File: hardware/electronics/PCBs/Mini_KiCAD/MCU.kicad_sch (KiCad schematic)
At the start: 21 parts, among them U1 RP2040, U2 W25Q32JVSS

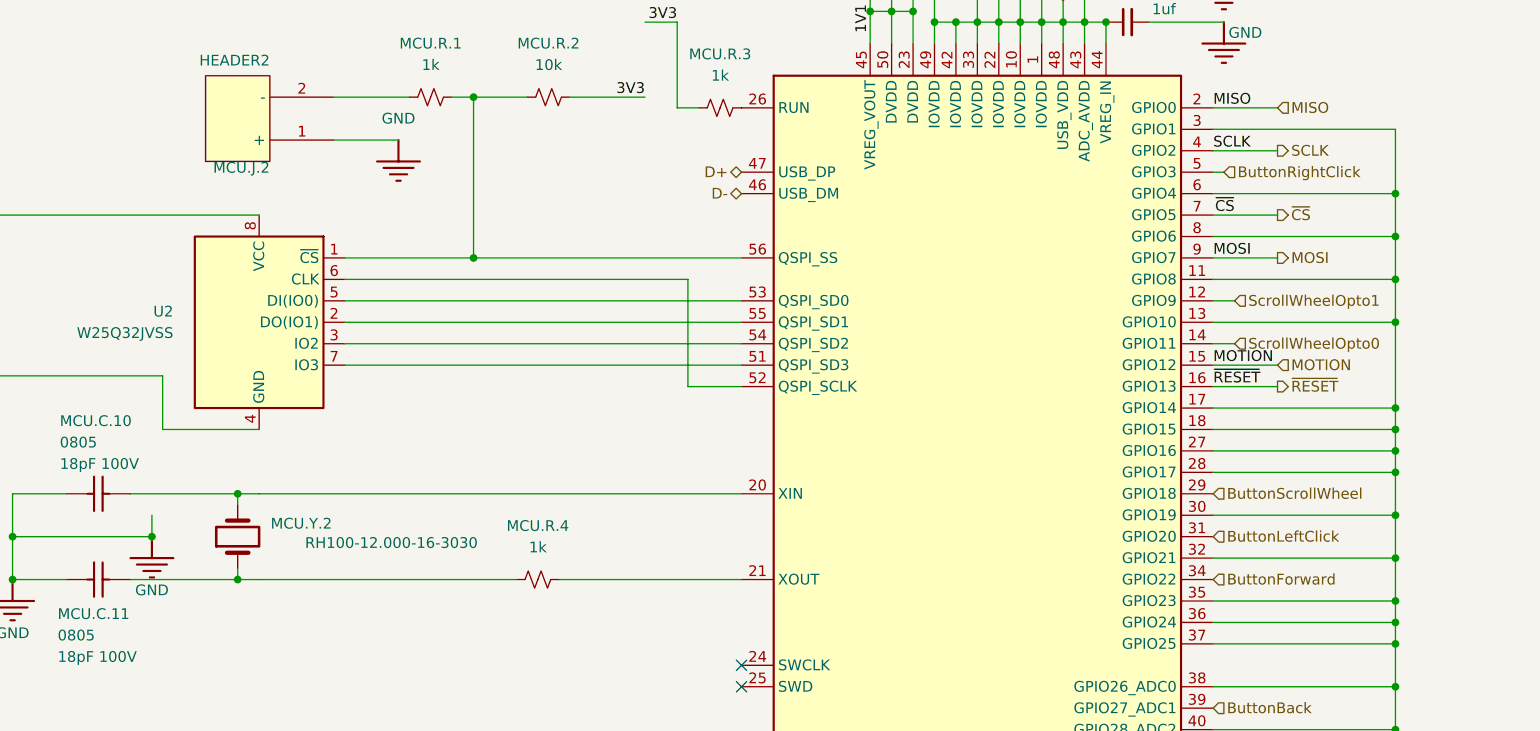
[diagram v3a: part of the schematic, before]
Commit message: Rerouted the SPI devices and general cleanup, relocated all associated footprint library inside the project folder
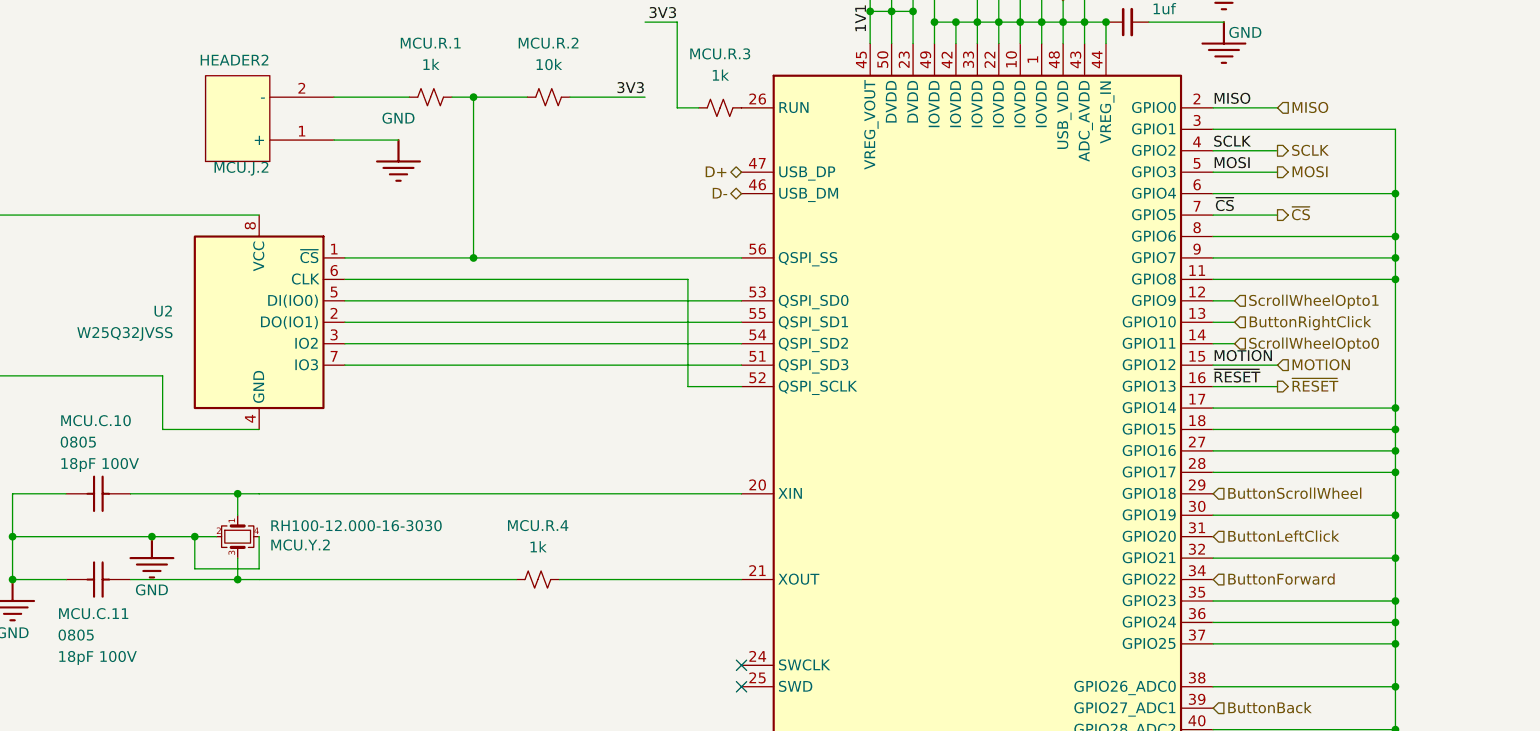
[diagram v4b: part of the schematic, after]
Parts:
- MCU.C.1, MCU.C.13, MCU.C.2, MCU.C.4, MCU.C.5, MCU.C.6, MCU.C.7, MCU.C.8, MCU.C.9: footprint Chip_Passives.PcbLib:0805 -> Chip_Passives.PcbLib:0805 - TALL
- MCU.Y.2: symbol Device:Crystal -> Device:Crystal_GND24_Small
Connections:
- net ButtonRightClick: now also U1.13 (GPIO10); no longer U1.5 (GPIO3)
- net GND: now also MCU.Y.2.2, MCU.Y.2.4, U1.9 (GPIO7); no longer U1.13 (GPIO10)
- net MOSI: now also U1.5 (GPIO3); no longer U1.9 (GPIO7)
- net at MCU.C.10.2, U1.20 (XIN): now also MCU.Y.2.1; no longer MCU.Y.2.2
- net at MCU.C.11.2, MCU.R.4.1: now also MCU.Y.2.3; no longer MCU.Y.2.1

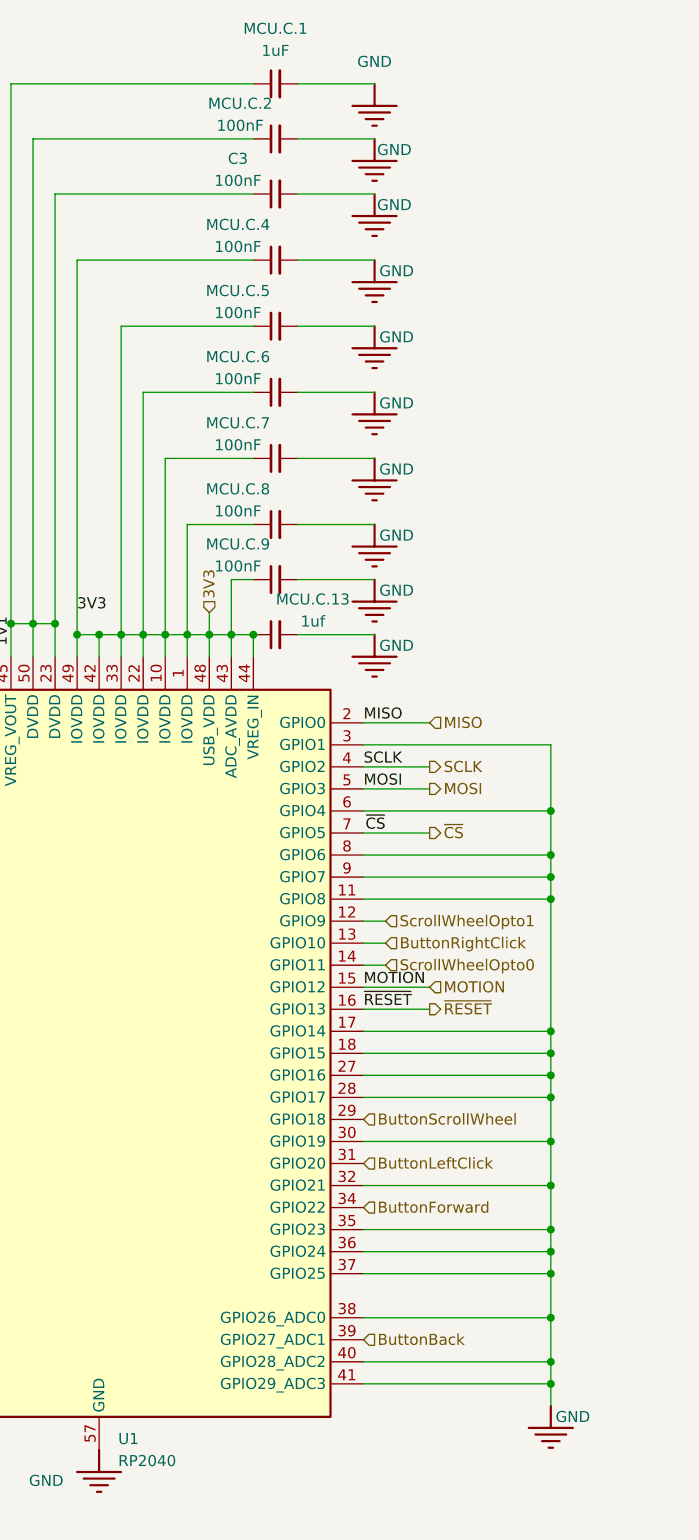
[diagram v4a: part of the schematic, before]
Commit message: Changed button and SPI device pinout to be pin-compatible with the Ploopy Adept.
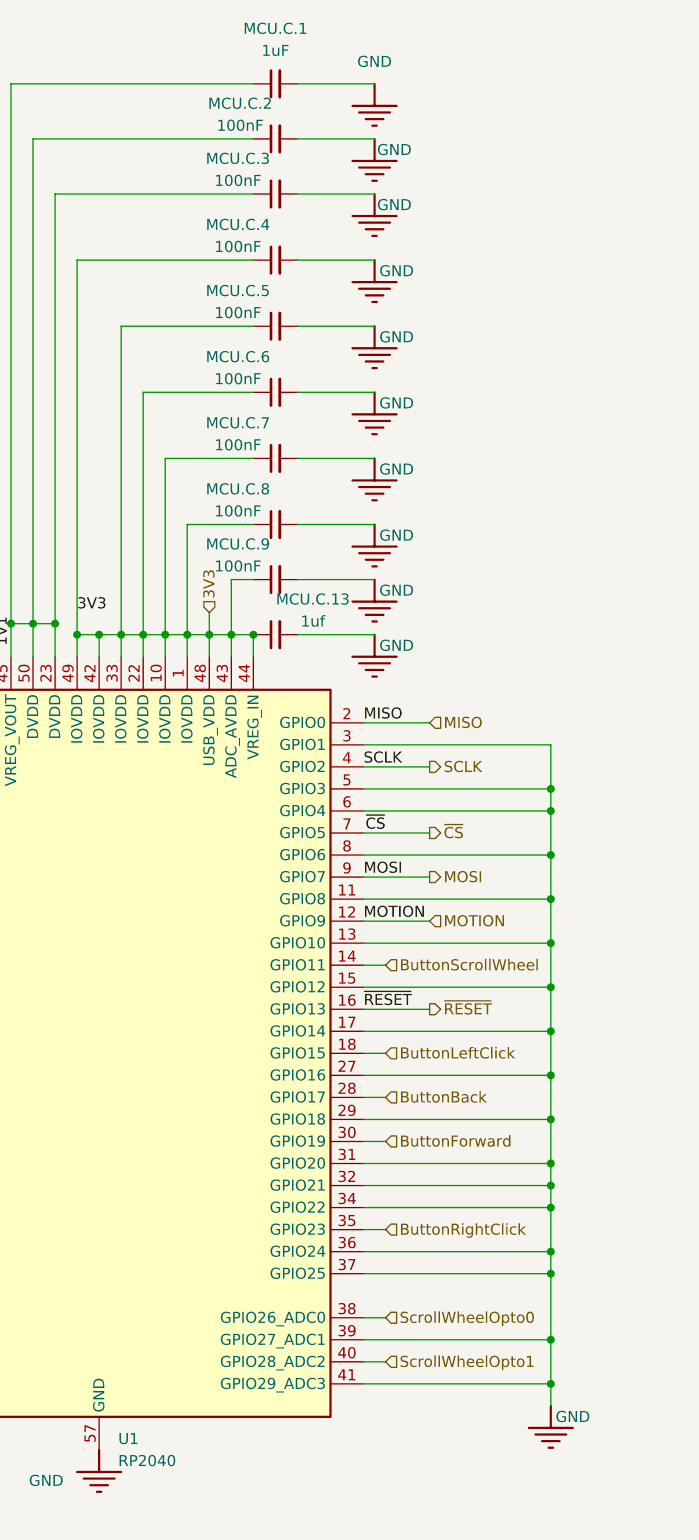
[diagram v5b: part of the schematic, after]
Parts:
- renumbered C3 to MCU.C.3
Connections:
- net ButtonBack: now also U1.28 (GPIO17); no longer U1.39 (GPIO27_ADC1)
- net ButtonForward: now also U1.30 (GPIO19); no longer U1.34 (GPIO22)
- net ButtonLeftClick: now also U1.18 (GPIO15); no longer U1.31 (GPIO20)
- net ButtonRightClick: now also U1.35 (GPIO23); no longer U1.13 (GPIO10)
- net ButtonScrollWheel: now also U1.14 (GPIO11); no longer U1.29 (GPIO18)
- net GND: now also U1.13 (GPIO10), U1.15 (GPIO12), U1.29 (GPIO18), U1.31 (GPIO20), U1.34 (GPIO22), U1.39 (GPIO27_ADC1), U1.5 (GPIO3); no longer U1.18 (GPIO15), U1.28 (GPIO17), U1.30 (GPIO19), U1.35 (GPIO23), U1.38 (GPIO26_ADC0), U1.40 (GPIO28_ADC2), U1.9 (GPIO7)
- net MOSI: now also U1.9 (GPIO7); no longer U1.5 (GPIO3)
- net MOTION: now also U1.12 (GPIO9); no longer U1.15 (GPIO12)
- net ScrollWheelOpto0: now also U1.38 (GPIO26_ADC0); no longer U1.14 (GPIO11)
- net ScrollWheelOpto1: now also U1.40 (GPIO28_ADC2); no longer U1.12 (GPIO9)

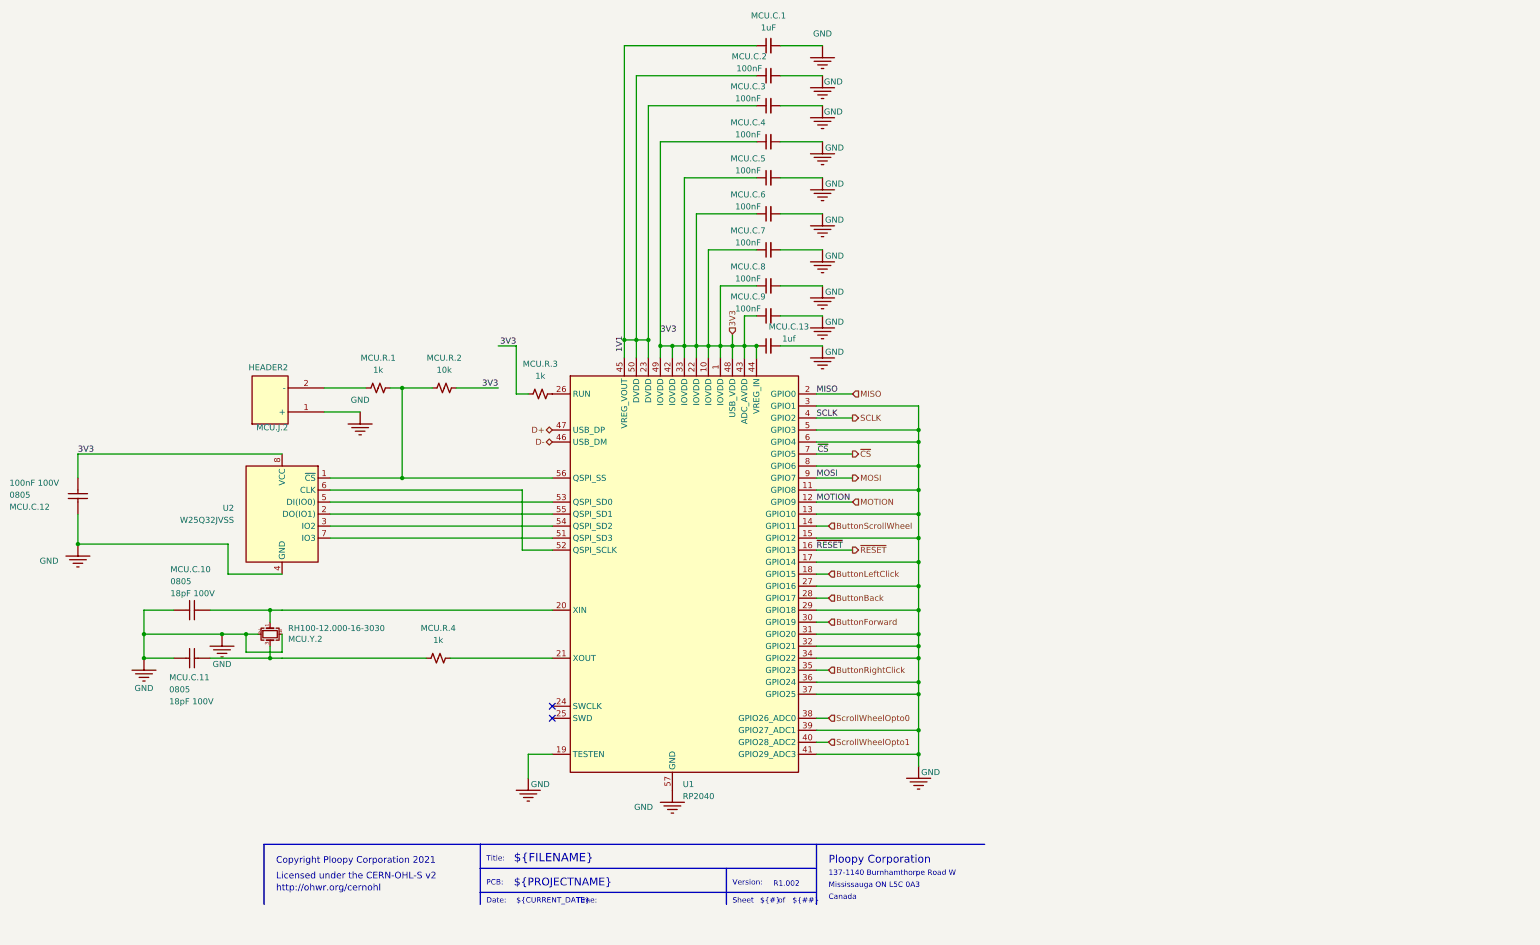
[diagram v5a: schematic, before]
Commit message: Resolved most DRC errors and re-annotated the schematic to be friendly to BOM generation.
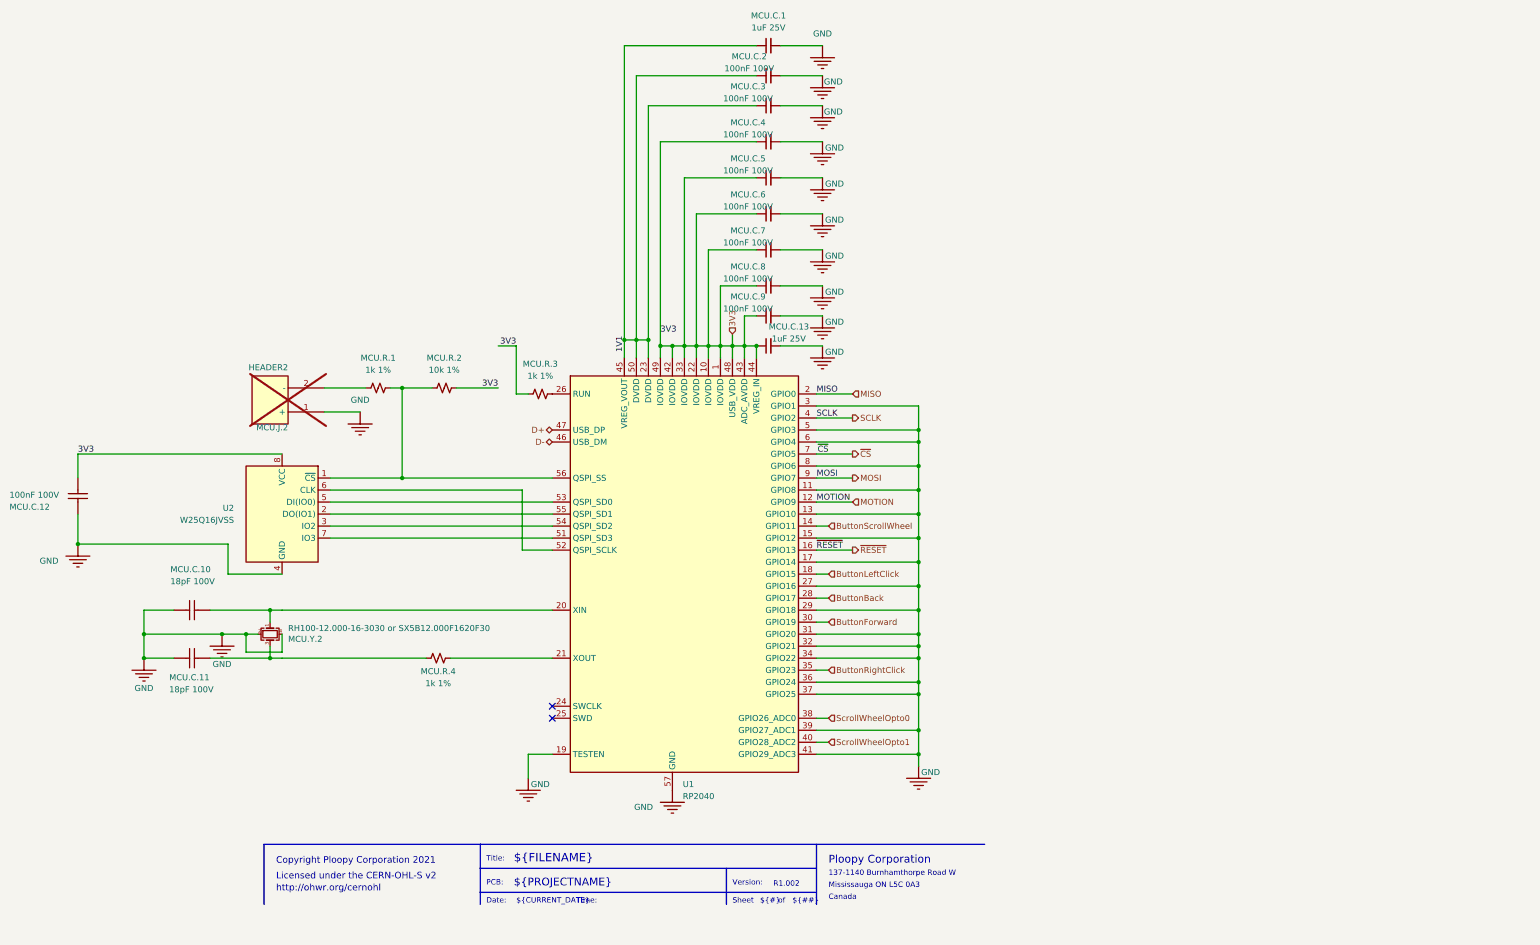
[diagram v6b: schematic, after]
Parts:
- MCU.C.1: value 1uF -> 1uF 25V
- MCU.C.10, MCU.C.11: value 0805 -> 18pF 100V
- MCU.C.12: value 0805 -> 100nF 100V
- MCU.C.13: value 1uf -> 1uF 25V
- MCU.C.2, MCU.C.3, MCU.C.4, MCU.C.5, MCU.C.6, MCU.C.7, MCU.C.8, MCU.C.9: value 100nF -> 100nF 100V
- MCU.J.2: now not fitted
- MCU.R.1, MCU.R.3, MCU.R.4: value 1k -> 1k 1%
- MCU.R.2: value 10k -> 10k 1%
- MCU.Y.2: value RH100-12.000-16-3030 -> RH100-12.000-16-3030 or SX5B12.000F1620F30
- U2: value W25Q32JVSS -> W25Q16JVSS
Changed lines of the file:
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@@
 			)
 		)
-		(property "Value" "1k"
+		(property "Value" "1k 1%"
 			(at 142.24 92.71 90)
 			(effects
@@
 			)
 		)
-		(property "Value" "0805"
+		(property "Value" "18pF 100V"
 			(at 64.008 136.906 90)
 			(effects
@@
 				)
 				(justify left bottom)
+				(hide yes)
 			)
 		)
@@
 			)
 		)
-		(property "Value" "100nF"
+		(property "Value" "100nF 100V"
 			(at 186.182 72.136 90)
 			(effects
@@
 			)
 		)
-		(property "Value" "RH100-12.000-16-3030"
+		(property "Value" "RH100-12.000-16-3030 or SX5B12.000F1620F30"
 			(at 88.9 146.812 90)
 			(effects
@@
 			)
 		)
-		(property "Value" "W25Q32JVSS"
+		(property "Value" "W25Q16JVSS"
 			(at 77.47 123.1899 0)
 			(effects
@@
 		(on_board yes)
 		(dnp no)
-		(fields_autoplaced yes)
 		(property "Reference" "MCU.R.4"
-			(at 120.65 146.05 90)
-			(effects
-				(font
-					(size 1.27 1.27)
-				)
-			)
-		)
-		(property "Value" "1k"
-			(at 120.65 148.59 90)
+			(at 120.65 155.194 90)
+			(effects
+				(font
+					(size 1.27 1.27)
+				)
+			)
+		)
+		(property "Value" "1k 1%"
+			(at 120.65 157.734 90)
 			(effects
 				(font
@@
 			)
 		)
-		(property "Value" "100nF"
+		(property "Value" "100nF 100V"
 			(at 186.182 41.656 90)
 			(effects
@@
 			)
 		)
-		(property "Value" "0805"
+		(property "Value" "18pF 100V"
 			(at 63.754 159.766 90)
 			(effects
@@
 				)
 				(justify left bottom)
+				(hide yes)
 			)
 		)
@@
 			)
 		)
-		(property "Value" "10k"
+		(property "Value" "10k 1%"
 			(at 121.92 91.44 90)
 			(effects
@@
 			)
 		)
-		(property "Value" "1uF"
+		(property "Value" "1uF 25V"
 			(at 190.5063 19.05 90)
 			(effects
@@
 			)
 		)
-		(property "Value" "100nF"
+		(property "Value" "100nF 100V"
 			(at 186.182 49.276 90)
 			(effects
@@
 			)
 		)
-		(property "Value" "1uf"
+		(property "Value" "1uF 25V"
 			(at 194.818 84.836 90)
 			(effects
@@
 			)
 		)
-		(property "Value" "100nF"
+		(property "Value" "100nF 100V"
 			(at 186.436 27.686 90)
 			(effects
@@
 		(in_bom yes)
 		(on_board yes)
-		(dnp no)
+		(dnp yes)
 		(property "Reference" "MCU.J.2"
 			(at 88.9 102.87 0)
@@
 			)
 		)
-		(property "Value" "100nF"
+		(property "Value" "100nF 100V"
 			(at 186.182 56.896 90)
 			(effects
@@
 			)
 		)
-		(property "Value" "100nF"
+		(property "Value" "100nF 100V"
 			(at 186.182 64.516 90)
 			(effects
@@
 			)
 		)
-		(property "Value" "100nF"
+		(property "Value" "100nF 100V"
 			(at 186.182 34.036 90)
 			(effects
@@
 			)
 		)
-		(property "Value" "100nF"
+		(property "Value" "100nF 100V"
 			(at 186.182 78.486 90)
 			(effects
@@
 			)
 		)
-		(property "Value" "1k"
+		(property "Value" "1k 1%"
 			(at 107.95 91.44 90)
 			(effects
@@
 			)
 		)
-		(property "Value" "0805"
+		(property "Value" "100nF 100V"
 			(at 29.972 118.618 0)
 			(effects
@@
 				)
 				(justify left bottom)
-			)
-		)
+				(hide yes)
+			)
+		)
